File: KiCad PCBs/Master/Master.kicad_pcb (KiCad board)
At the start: 2 copper layers, 80.6 x 55.2 mm, 21 parts

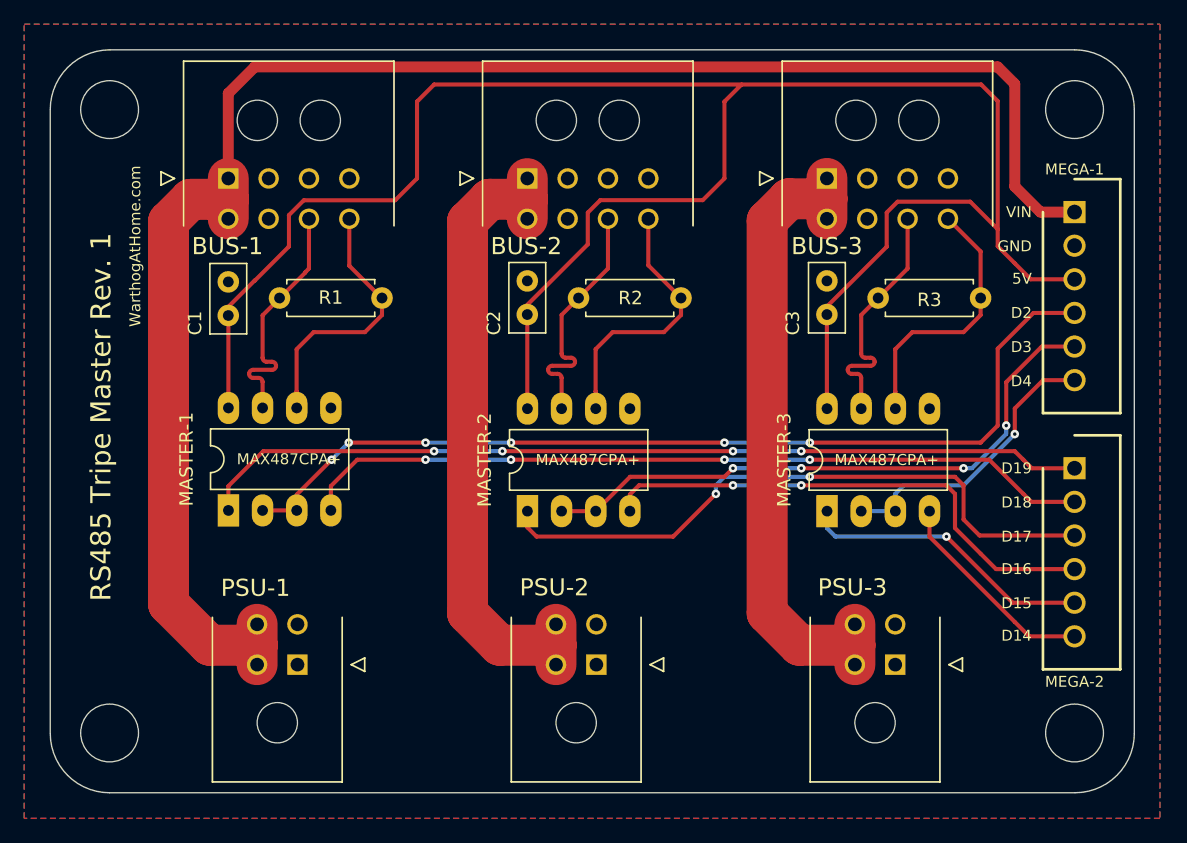
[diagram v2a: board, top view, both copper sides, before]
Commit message: Modified mounting holes to M3
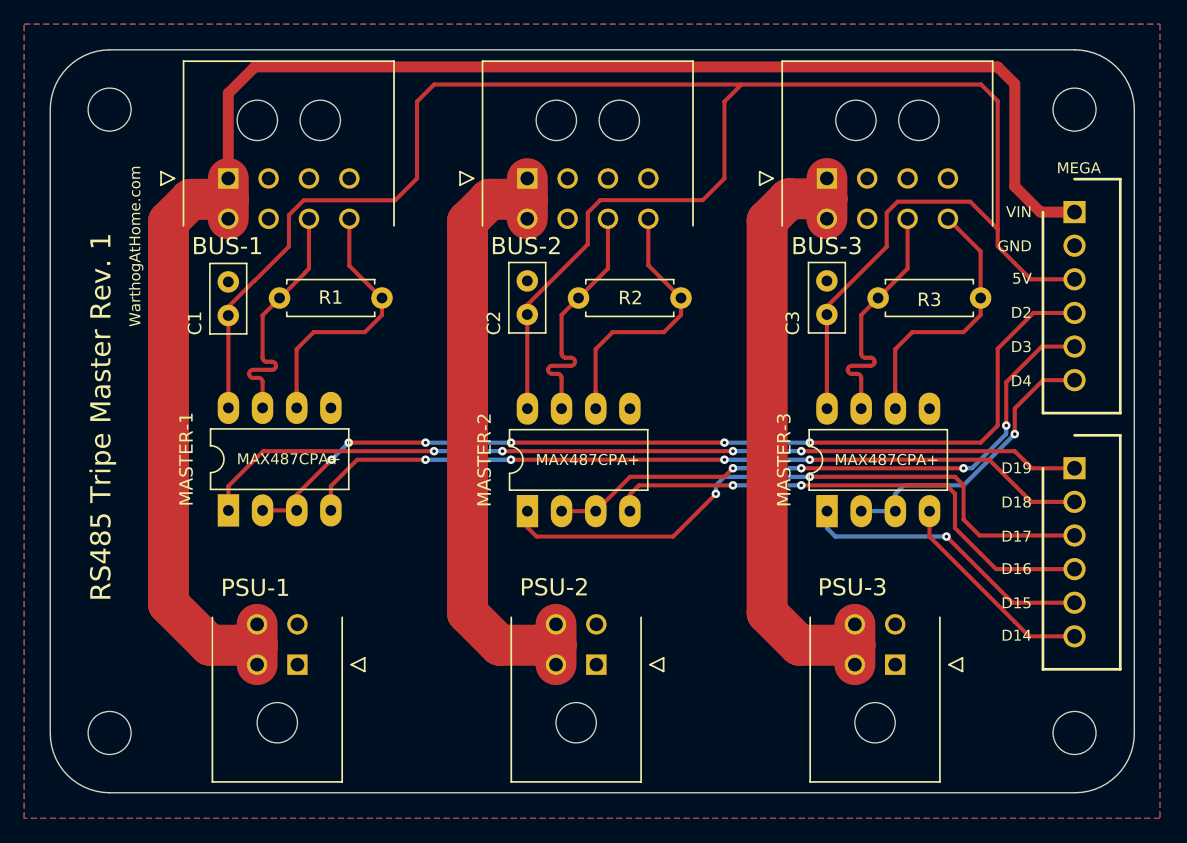
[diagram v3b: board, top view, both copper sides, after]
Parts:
- REF** (x4): value MountingHole_4.3mm_M4 -> MountingHole_3.2mm_M3; footprint MountingHole:MountingHole_4.3mm_M4 -> MountingHole:MountingHole_3.2mm_M3
- renumbered MEGA-1 to MEGA
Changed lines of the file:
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@@
   (net 25 "unconnected-(BUS-3-Pad3)")
   (net 26 "unconnected-(BUS-3-Pad4)")
-  (footprint "MountingHole:MountingHole_4.3mm_M4" (layer "F.Cu")
+  (footprint "MountingHole:MountingHole_3.2mm_M3" (layer "F.Cu")
     (at 99.695 26.67)
-    (descr "Mounting Hole 4.3mm, no annular, M4")
-    (tags "mounting hole 4.3mm no annular m4")
-    (attr board_only exclude_from_pos_files exclude_from_bom)
-    (fp_text reference "REF**" (at 0 -5.3) (layer "F.SilkS") hide
-      (effects (font (size 1 1) (thickness 0.15)))
-    )
-    (fp_text value "MountingHole_4.3mm_M4" (at 0 5.3) (layer "F.Fab") hide
+    (descr "Mounting Hole 3.2mm, no annular, M3")
+    (tags "mounting hole 3.2mm no annular m3")
+    (attr exclude_from_pos_files exclude_from_bom)
+    (fp_text reference "REF**" (at 0 -4.2) (layer "F.SilkS") hide
+      (effects (font (size 1 1) (thickness 0.15)))
+    )
+    (fp_text value "MountingHole_3.2mm_M3" (at 0 4.2) (layer "F.Fab") hide
       (effects (font (size 1 1) (thickness 0.15)))
     )
@@
       (effects (font (size 1 1) (thickness 0.15)))
     )
-    (fp_circle (center 0 0) (end 4.3 0) (layer "Cmts.User") (width 0.15) (fill none))
-    (fp_circle (center 0 0) (end 4.55 0) (layer "F.CrtYd") (width 0.05) (fill none))
-    (pad "" np_thru_hole circle (at 0 0) (size 4.3 4.3) (drill 4.3) (layers *.Cu *.Mask))
+    (fp_circle (center 0 0) (end 3.2 0) (layer "Cmts.User") (width 0.15) (fill none))
+    (fp_circle (center 0 0) (end 3.45 0) (layer "F.CrtYd") (width 0.05) (fill none))
+    (pad "" np_thru_hole circle (at 0 0) (size 3.2 3.2) (drill 3.2) (layers *.Cu *.Mask))
   )
   (footprint "Capacitor_THT:C_Disc_D5.0mm_W2.5mm_P2.50mm" (layer "F.Cu")
@@
     )
   )
-  (footprint "MountingHole:MountingHole_4.3mm_M4" (layer "F.Cu")
+  (footprint "MountingHole:MountingHole_3.2mm_M3" (layer "F.Cu")
     (at 99.695 73.025)
-    (descr "Mounting Hole 4.3mm, no annular, M4")
-    (tags "mounting hole 4.3mm no annular m4")
-    (attr board_only exclude_from_pos_files exclude_from_bom)
-    (fp_text reference "REF**" (at 0 -5.3) (layer "F.SilkS") hide
-      (effects (font (size 1 1) (thickness 0.15)))
-    )
-    (fp_text value "MountingHole_4.3mm_M4" (at 0 5.3) (layer "F.Fab") hide
+    (descr "Mounting Hole 3.2mm, no annular, M3")
+    (tags "mounting hole 3.2mm no annular m3")
+    (attr exclude_from_pos_files exclude_from_bom)
+    (fp_text reference "REF**" (at 0 -4.2) (layer "F.SilkS") hide
+      (effects (font (size 1 1) (thickness 0.15)))
+    )
+    (fp_text value "MountingHole_3.2mm_M3" (at 0 4.2) (layer "F.Fab") hide
       (effects (font (size 1 1) (thickness 0.15)))
     )
@@
       (effects (font (size 1 1) (thickness 0.15)))
     )
-    (fp_circle (center 0 0) (end 4.3 0) (layer "Cmts.User") (width 0.15) (fill none))
-    (fp_circle (center 0 0) (end 4.55 0) (layer "F.CrtYd") (width 0.05) (fill none))
-    (pad "" np_thru_hole circle (at 0 0) (size 4.3 4.3) (drill 4.3) (layers *.Cu *.Mask))
+    (fp_circle (center 0 0) (end 3.2 0) (layer "Cmts.User") (width 0.15) (fill none))
+    (fp_circle (center 0 0) (end 3.45 0) (layer "F.CrtYd") (width 0.05) (fill none))
+    (pad "" np_thru_hole circle (at 0 0) (size 3.2 3.2) (drill 3.2) (layers *.Cu *.Mask))
   )
   (footprint "A10 KiCad Libraries:SHDR6W64P0X250_1X6_1740X575X700P" (layer "F.Cu")
@@
     (property "Sheetname" "")
     (attr through_hole)
-    (fp_text reference "MEGA-2" (at 15.875 0 180) (layer "F.SilkS")
+    (fp_text reference "MEGA-2" (at 15.875 0 180) (layer "F.SilkS") hide
       (effects (font (size 0.8128 0.8128) (thickness 0.2032)))
     )
@@
       (effects (font (size 1.27 1.27) (thickness 0.254)))
     )
-    (fp_text user "${REFERENCE}" (at 0 0 90) (layer "F.Fab")
+    (fp_text user "${REFERENCE}" (at 0 0 90) (layer "F.Fab") hide
       (effects (font (size 1.27 1.27) (thickness 0.254)))
     )
@@
     )
   )
-  (footprint "MountingHole:MountingHole_4.3mm_M4" (layer "F.Cu")
+  (footprint "MountingHole:MountingHole_3.2mm_M3" (layer "F.Cu")
     (at 27.94 26.67)
-    (descr "Mounting Hole 4.3mm, no annular, M4")
-    (tags "mounting hole 4.3mm no annular m4")
-    (attr board_only exclude_from_pos_files exclude_from_bom)
-    (fp_text reference "REF**" (at 0 -5.3) (layer "F.SilkS") hide
-      (effects (font (size 1 1) (thickness 0.15)))
-    )
-    (fp_text value "MountingHole_4.3mm_M4" (at 0 5.3) (layer "F.Fab") hide
+    (descr "Mounting Hole 3.2mm, no annular, M3")
+    (tags "mounting hole 3.2mm no annular m3")
+    (attr exclude_from_pos_files exclude_from_bom)
+    (fp_text reference "REF**" (at 0 -4.2) (layer "F.SilkS") hide
+      (effects (font (size 1 1) (thickness 0.15)))
+    )
+    (fp_text value "MountingHole_3.2mm_M3" (at 0 4.2) (layer "F.Fab") hide
       (effects (font (size 1 1) (thickness 0.15)))
     )
@@
       (effects (font (size 1 1) (thickness 0.15)))
     )
-    (fp_circle (center 0 0) (end 4.3 0) (layer "Cmts.User") (width 0.15) (fill none))
-    (fp_circle (center 0 0) (end 4.55 0) (layer "F.CrtYd") (width 0.05) (fill none))
-    (pad "" np_thru_hole circle (at 0 0) (size 4.3 4.3) (drill 4.3) (layers *.Cu *.Mask))
+    (fp_circle (center 0 0) (end 3.2 0) (layer "Cmts.User") (width 0.15) (fill none))
+    (fp_circle (center 0 0) (end 3.45 0) (layer "F.CrtYd") (width 0.05) (fill none))
+    (pad "" np_thru_hole circle (at 0 0) (size 3.2 3.2) (drill 3.2) (layers *.Cu *.Mask))
   )
   (footprint "A10 KiCad Libraries:Molex 43045-0800" (layer "F.Cu")
@@
     (property "Sheetname" "")
     (attr through_hole)
-    (fp_text reference "MEGA-1" (at -3.175 0 180) (layer "F.SilkS")
+    (fp_text reference "MEGA" (at -3.262772 -0.317145 180) (layer "F.SilkS")
       (effects (font (size 0.8128 0.8128) (thickness 0.2032)))
     )
@@
       (effects (font (size 1.27 1.27) (thickness 0.254)))
     )
-    (fp_text user "${REFERENCE}" (at 0 0 90) (layer "F.Fab")
+    (fp_text user "${REFERENCE}" (at 0 0 90) (layer "F.Fab") hide
       (effects (font (size 1.27 1.27) (thickness 0.254)))
     )
@@
     )
   )
-  (footprint "MountingHole:MountingHole_4.3mm_M4" (layer "F.Cu")
+  (footprint "MountingHole:MountingHole_3.2mm_M3" (layer "F.Cu")
     (at 27.94 73.025)
-    (descr "Mounting Hole 4.3mm, no annular, M4")
-    (tags "mounting hole 4.3mm no annular m4")
-    (attr board_only exclude_from_pos_files exclude_from_bom)
-    (fp_text reference "REF**" (at 0 -5.3) (layer "F.SilkS") hide
-      (effects (font (size 1 1) (thickness 0.15)))
-    )
-    (fp_text value "MountingHole_4.3mm_M4" (at 0 5.3) (layer "F.Fab") hide
+    (descr "Mounting Hole 3.2mm, no annular, M3")
+    (tags "mounting hole 3.2mm no annular m3")
+    (attr exclude_from_pos_files exclude_from_bom)
+    (fp_text reference "REF**" (at 0 -4.2) (layer "F.SilkS") hide
+      (effects (font (size 1 1) (thickness 0.15)))
+    )
+    (fp_text value "MountingHole_3.2mm_M3" (at 0 4.2) (layer "F.Fab") hide
       (effects (font (size 1 1) (thickness 0.15)))
     )
@@
       (effects (font (size 1 1) (thickness 0.15)))
     )
-    (fp_circle (center 0 0) (end 4.3 0) (layer "Cmts.User") (width 0.15) (fill none))
-    (fp_circle (center 0 0) (end 4.55 0) (layer "F.CrtYd") (width 0.05) (fill none))
-    (pad "" np_thru_hole circle (at 0 0) (size 4.3 4.3) (drill 4.3) (layers *.Cu *.Mask))
+    (fp_circle (center 0 0) (end 3.2 0) (layer "Cmts.User") (width 0.15) (fill none))
+    (fp_circle (center 0 0) (end 3.45 0) (layer "F.CrtYd") (width 0.05) (fill none))
+    (pad "" np_thru_hole circle (at 0 0) (size 3.2 3.2) (drill 3.2) (layers *.Cu *.Mask))
   )
   (footprint "Capacitor_THT:C_Disc_D5.0mm_W2.5mm_P2.50mm" (layer "F.Cu")

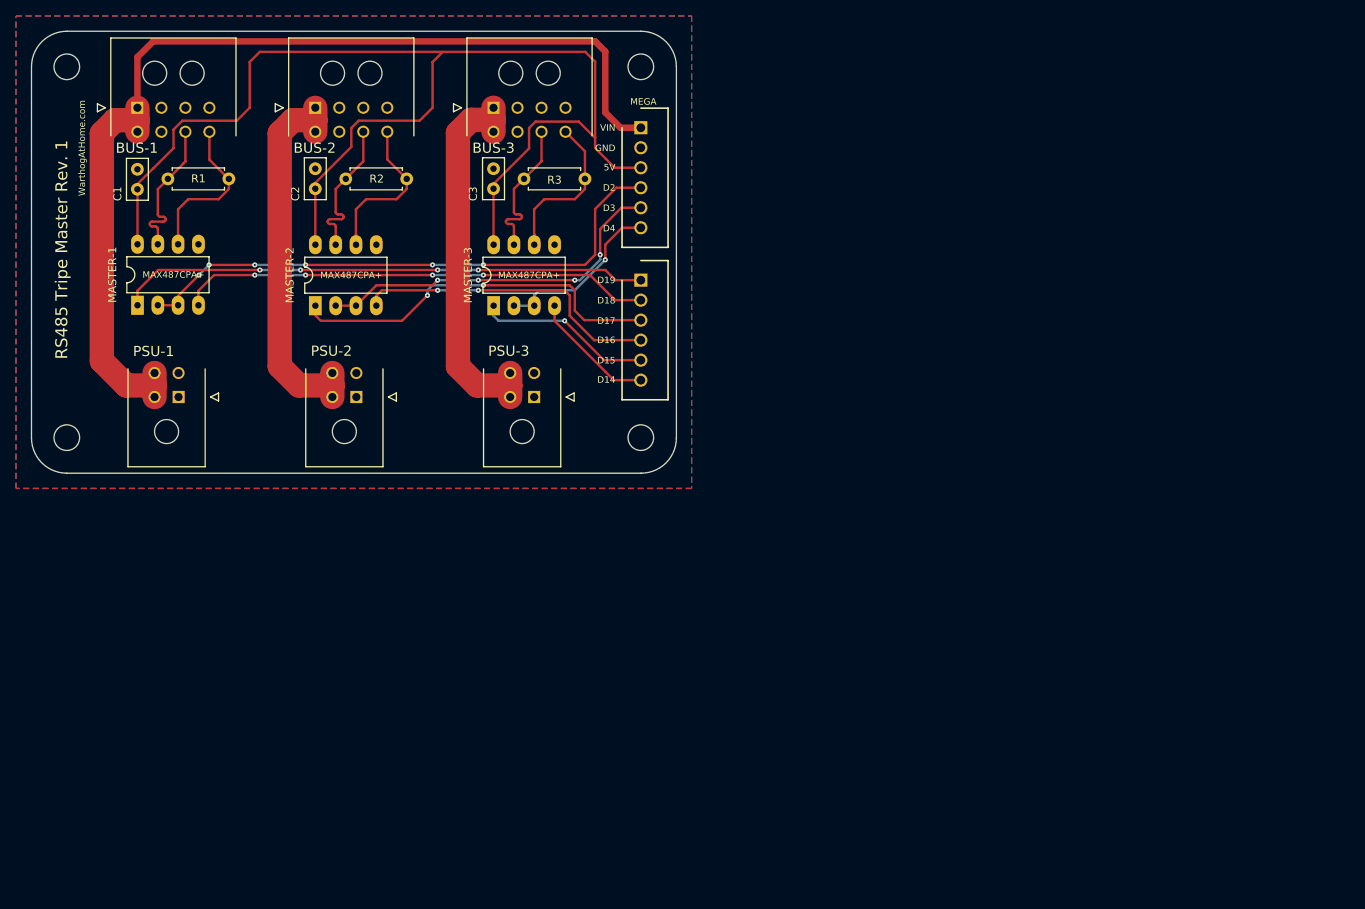
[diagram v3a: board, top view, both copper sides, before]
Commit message: Added Micro Blade fuse holder to each bus Updated cap 3d model Ignored KiCad backups
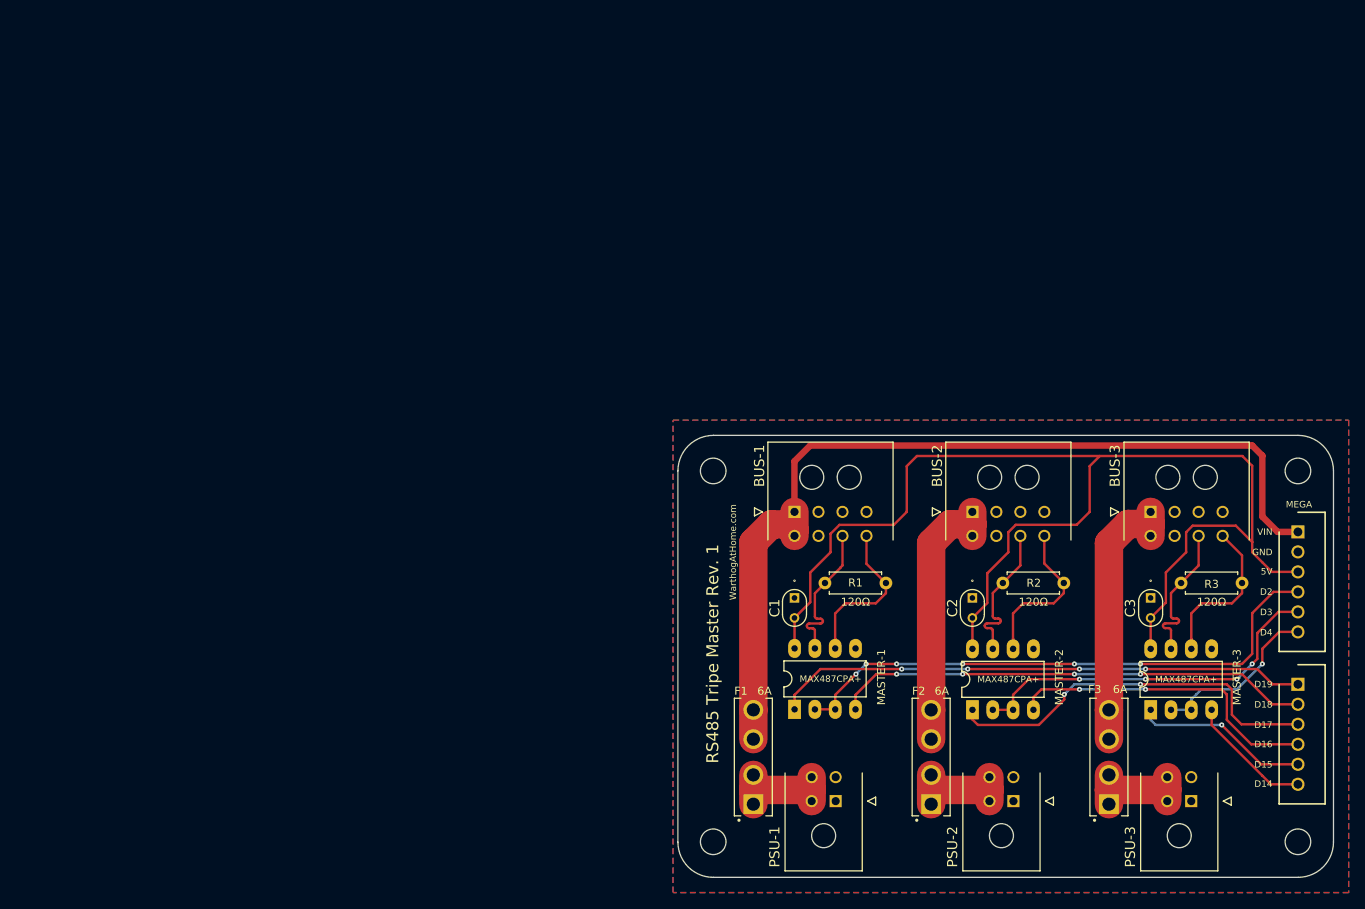
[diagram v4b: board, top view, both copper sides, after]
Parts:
- added F1: 6A, A10 KiCad Libraries:FUSE_BK-6013, F.Cu at (113.8, 112.9)
- added F2: 6A, A10 KiCad Libraries:FUSE_BK-6013, F.Cu at (136.0, 112.9)
- added F3: 6A, A10 KiCad Libraries:FUSE_BK-6013, F.Cu at (158.2, 112.9)
- C1, C2, C3: footprint Capacitor_THT:C_Disc_D5.0mm_W2.5mm_P2.50mm -> A10 KiCad Libraries:FA14
- moved C2 98.1 mm to (141.1, 93.1)
- moved C3 98.1 mm to (163.4, 93.1)
- moved C1 98.1 mm to (118.9, 93.1)
- moved HOLE-2 96.4 mm to (181.8, 77.2)
- moved HOLE-4 96.4 mm to (181.8, 123.5)
- moved MASTER-2 96.4 mm to (141.1, 107.0)
- moved MEGA-1 96.4 mm to (181.8, 84.8)
- moved MEGA-2 96.4 mm to (181.8, 103.9)
- moved BUS-1 96.4 mm to (118.9, 82.3)
- moved MASTER-3 96.4 mm to (163.4, 107.0)
- moved PSU-1 96.4 mm to (124.0, 118.5)
- moved PSU-2 96.4 mm to (146.3, 118.5)
- moved PSU-3 96.4 mm to (168.5, 118.5)
- moved BUS-2 96.4 mm to (141.1, 82.3)
- moved BUS-3 96.4 mm to (163.4, 82.3)
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- renumbered REF** to HOLE-1, REF** to HOLE-2, REF** to HOLE-3, REF** to HOLE-4, MEGA to MEGA-1
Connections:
- BUS-1 pad 1: +12V -> 12V_Fused
- BUS-1 pad 5: +12V -> 12V_Fused
- BUS-2 pad 1: +12V_2 -> /12V_2_Fused
- BUS-2 pad 5: +12V_2 -> /12V_2_Fused
- BUS-3 pad 1: +12V_3 -> /12V_3_Fused
- BUS-3 pad 5: +12V_3 -> /12V_3_Fused
- MEGA-1 pad 1: +12V -> 12V_Fused
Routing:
- net 12V_Fused: track 0.00 -> 113.0 mm
- net +12V: track 126.4 -> 13.9 mm
- net +12V_2: track 47.8 -> 14.0 mm
- net +12V_3: track 47.8 -> 14.0 mm
- net /12V_3_Fused: track 0.00 -> 33.7 mm
- net /12V_2_Fused: track 0.00 -> 33.7 mm
- net MEGA_D16: track 38.7 -> 39.7 mm
- net MEGA_D17: track 47.7 -> 48.6 mm
- net MEGA_D3: track 45.5 -> 46.2 mm
- net MEGA_D19: track 66.3 -> 66.9 mm
- net MEGA_D18: track 59.2 -> 59.7 mm
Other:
- board size 80.6 x 55.2 mm -> 81.9 x 55.2 mm
